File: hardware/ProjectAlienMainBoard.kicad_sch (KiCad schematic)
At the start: 53 parts, among them J1 Bumper, J10 Excess GPIO Pins, J3 Left Motor, J4 Right Motor, J5 Pixels, J6 Ultrasonic, J7 Micro USB, J8 I2C Multiplexer, J9 Voltage Breakout, Q1 2N3904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

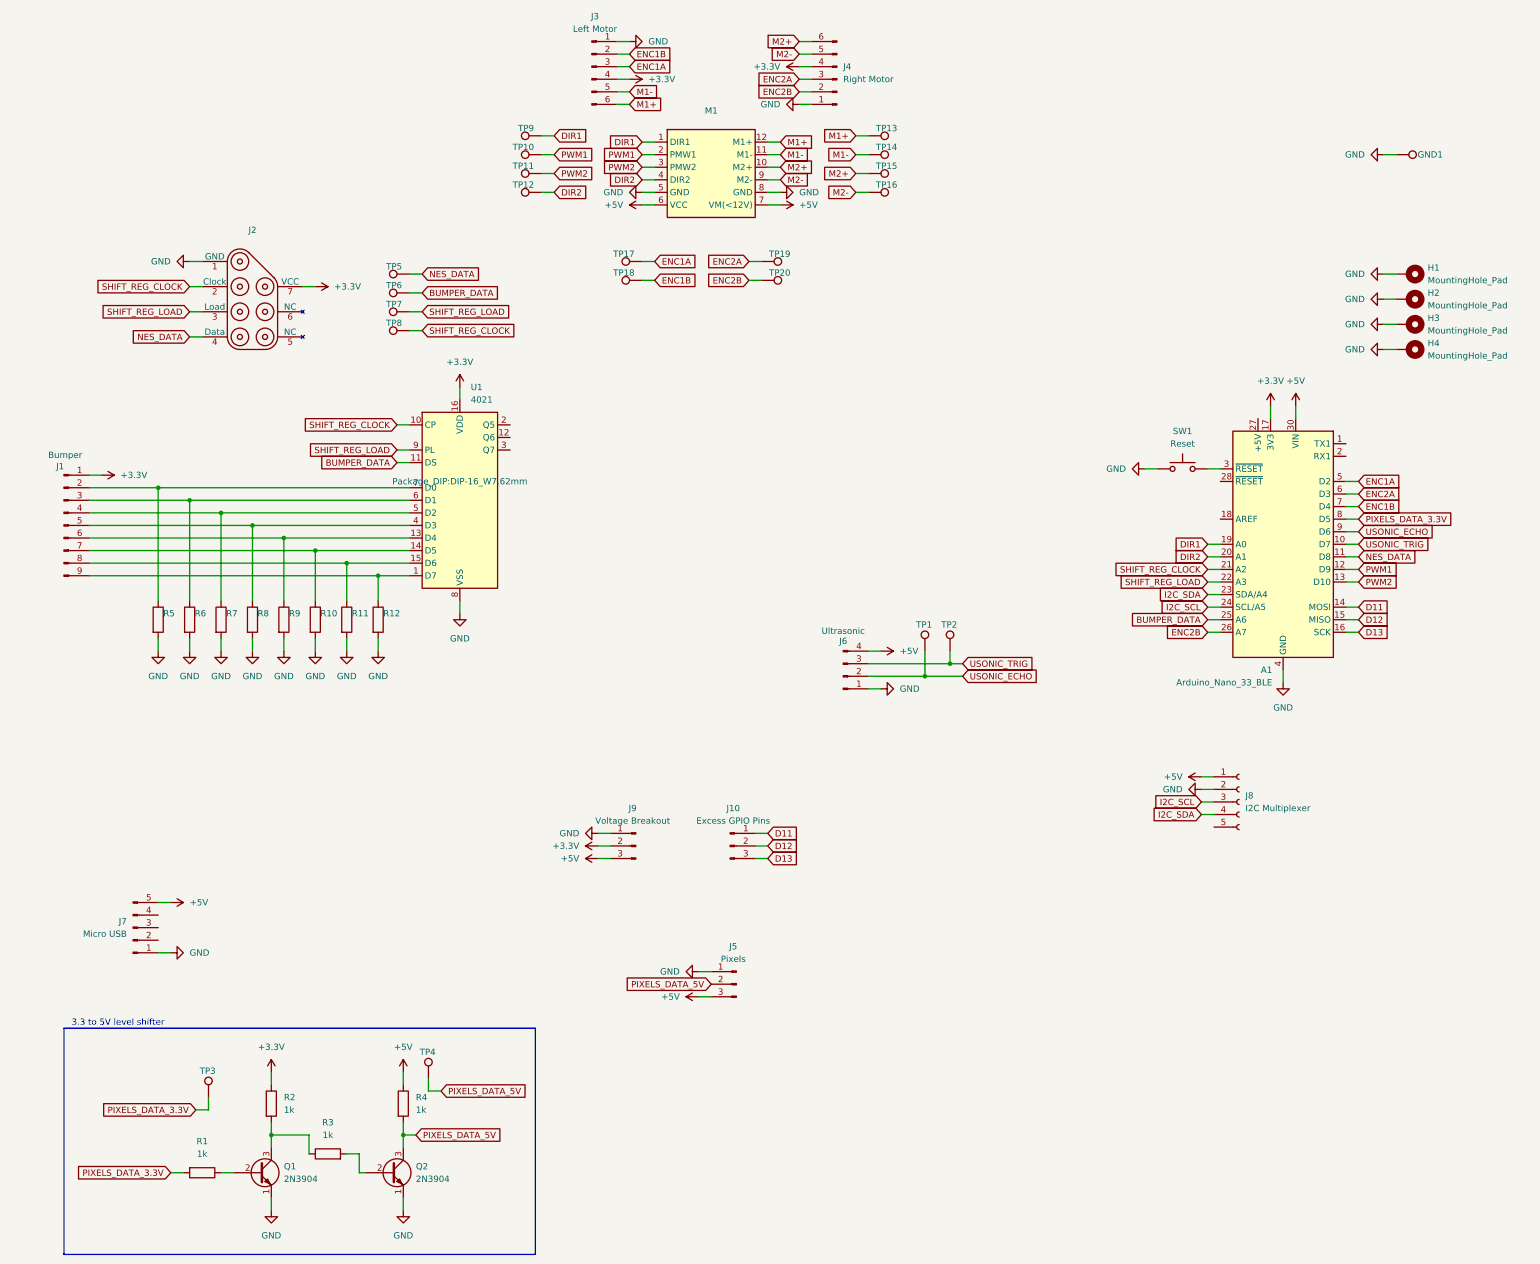
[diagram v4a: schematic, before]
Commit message: Tweaked silkscreen
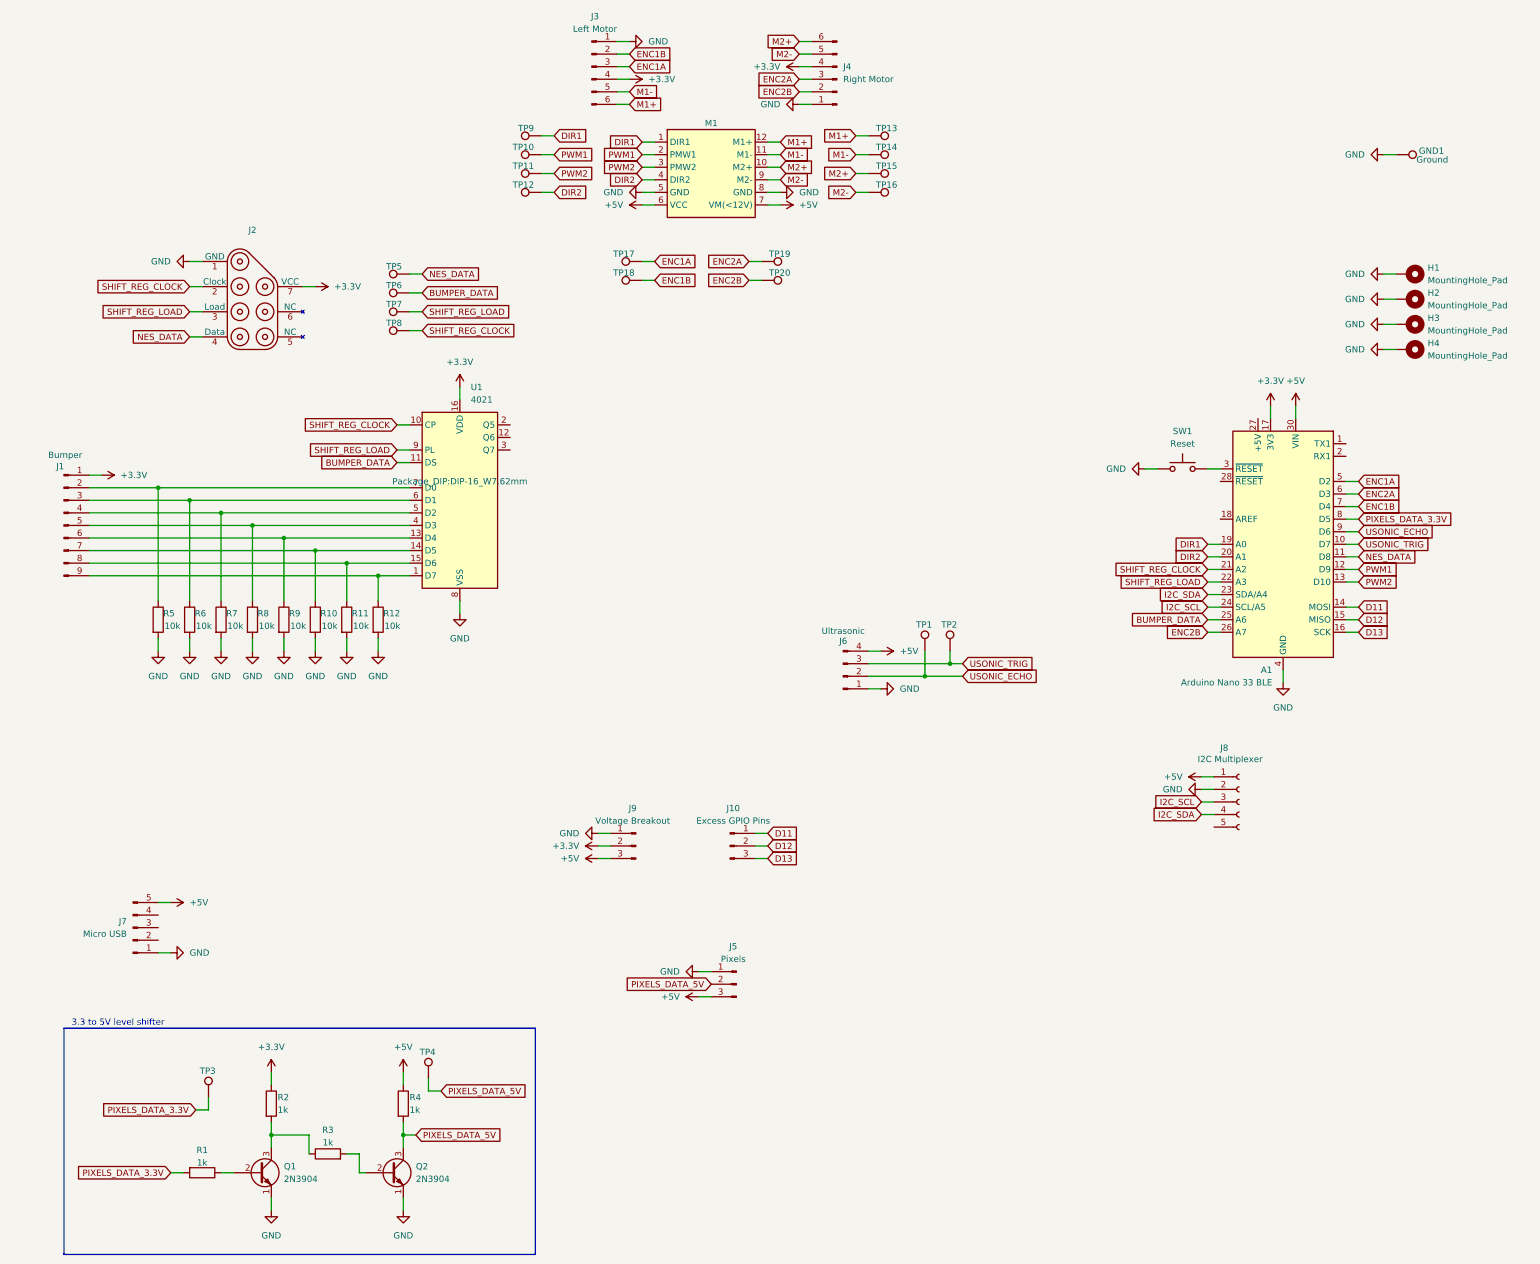
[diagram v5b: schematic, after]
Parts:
- A1: value Arduino_Nano_33_BLE -> Arduino Nano 33 BLE
- GND1: value GND -> Ground
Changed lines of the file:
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@@
 		(dnp no)
 		(property "Reference" "GND1"
-			(at 295.148 50.8 90)
+			(at 295.402 50.038 90)
 			(effects
 				(font
@@
 			)
 		)
-		(property "Value" "GND"
-			(at 295.91 52.0699 90)
+		(property "Value" "Ground"
+			(at 294.894 51.816 90)
 			(effects
 				(font
@@
 				)
 				(justify left)
-				(hide yes)
 			)
 		)
@@
 				)
 				(justify left)
-				(hide yes)
 			)
 		)
@@
 				)
 				(justify left)
-				(hide yes)
 			)
 		)
@@
 		(on_board yes)
 		(dnp no)
-		(fields_autoplaced yes)
 		(property "Reference" "R1"
-			(at 49.53 250.19 90)
+			(at 49.53 251.968 90)
 			(effects
 				(font
@@
 		)
 		(property "Value" "1k"
-			(at 49.53 252.73 90)
+			(at 49.53 254.508 90)
 			(effects
 				(font
@@
 				)
 				(justify left)
-				(hide yes)
 			)
 		)
@@
 		(on_board yes)
 		(dnp no)
-		(fields_autoplaced yes)
 		(property "Reference" "R4"
-			(at 92.71 241.2999 0)
+			(at 91.44 241.3 0)
 			(effects
 				(font
@@
 		)
 		(property "Value" "1k"
-			(at 92.71 243.8399 0)
+			(at 91.44 243.84 0)
 			(effects
 				(font
@@
 		(on_board yes)
 		(dnp no)
-		(fields_autoplaced yes)
 		(property "Reference" "M1"
-			(at 152.4 41.91 0)
+			(at 152.4 44.45 0)
 			(effects
 				(font
@@
 			)
 		)
-		(property "Value" "Arduino_Nano_33_BLE"
+		(property "Value" "Arduino Nano 33 BLE"
 			(at 265.7759 157.48 0)
 			(effects
@@
 		(on_board yes)
 		(dnp no)
-		(fields_autoplaced yes)
 		(property "Reference" "R2"
-			(at 66.04 241.2999 0)
+			(at 64.77 241.3 0)
 			(effects
 				(font
@@
 		)
 		(property "Value" "1k"
-			(at 66.04 243.8399 0)
+			(at 64.77 243.84 0)
 			(effects
 				(font
@@
 				)
 				(justify left)
-				(hide yes)
 			)
 		)
@@
 				)
 				(justify left)
-				(hide yes)
 			)
 		)
@@
 				)
 				(justify left)
-				(hide yes)
 			)
 		)
@@
 		(on_board yes)
 		(dnp no)
-		(fields_autoplaced yes)
 		(property "Reference" "J8"
-			(at 260.35 180.3399 0)
+			(at 255.27 170.688 0)
 			(effects
 				(font
@@
 		)
 		(property "Value" "I2C Multiplexer"
-			(at 260.35 182.8799 0)
+			(at 250.698 172.974 0)
 			(effects
 				(font
@@
 				)
 				(justify left)
-				(hide yes)
 			)
 		)
@@
 		(on_board yes)
 		(dnp no)
-		(fields_autoplaced yes)
 		(property "Reference" "R3"
-			(at 74.93 246.38 90)
+			(at 74.93 247.904 90)
 			(effects
 				(font
@@
 		)
 		(property "Value" "1k"
-			(at 74.93 248.92 90)
+			(at 74.93 250.444 90)
 			(effects
 				(font
@@
 				)
 				(justify left)
-				(hide yes)
 			)
 		)
